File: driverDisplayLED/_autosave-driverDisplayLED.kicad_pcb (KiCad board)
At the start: 2 copper layers, 59 parts, among them J1 Conn_01x12_Male, J10 Conn_01x12_Male, J11 Conn_01x12_Male, J12 Conn_01x12_Male, J13 Conn_01x12_Male, J14 Conn_01x12_Male, J15 Conn_01x12_Male, J16 Conn_01x12_Male, J17 Conn_01x12_Male, J2 Conn_01x12_Male, J3 Conn_01x12_Male, J4 Conn_02x08_Counter_Clockwise, J5 Conn_01x12_Male, J6 Conn_01x12_Male, J7 Conn_01x12_Male, J8 Conn_01x12_Male, J9 Conn_01x12_Male, Q1 FDS4953, Q2 FDS4953, Q3 FDS4953, Q4 FDS4953, Q5 FDS4953, Q6 FDS4953, Q7 FDS4953, Q8 FDS4953, U1 74HC245, U2 74HC595, U3 74HC595, U4 74HC245, U5 74HC138D, U6 74HC04, U7 74HC595, U8 74HC595, U9 74HC138D

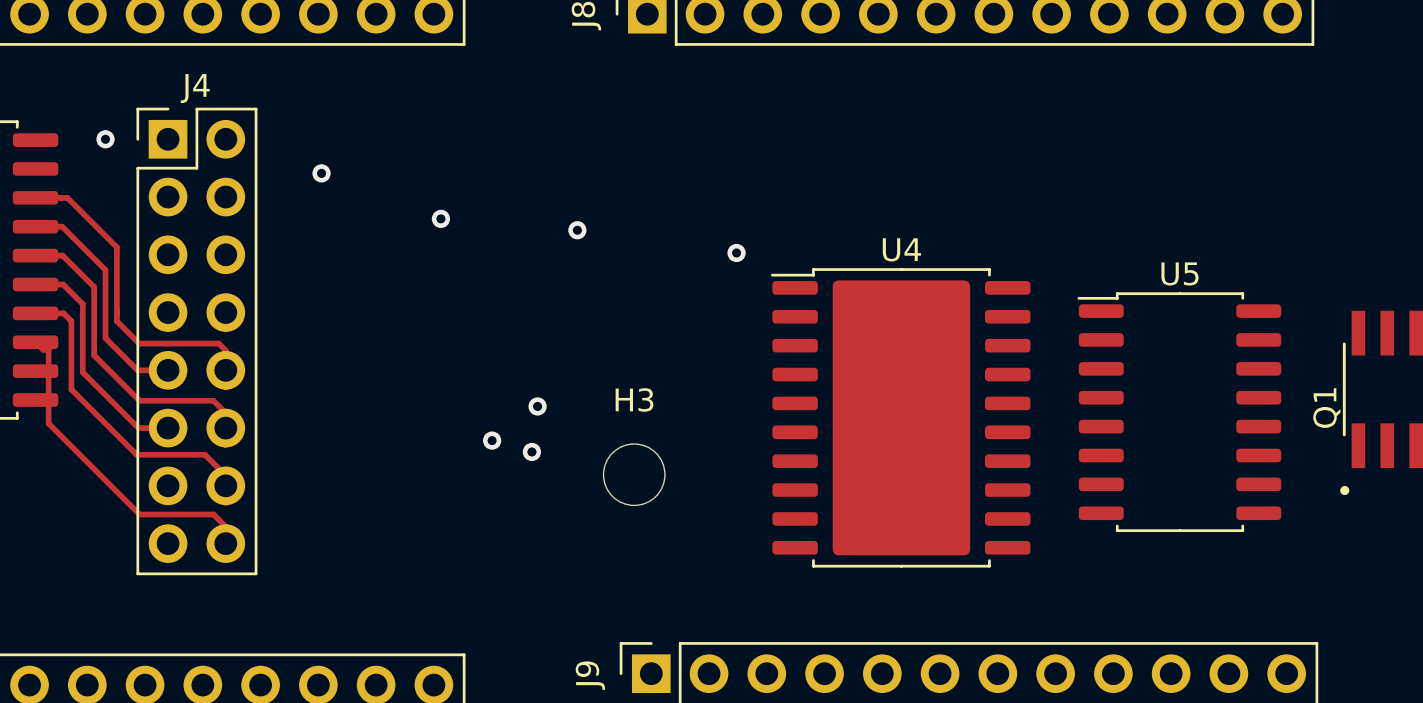
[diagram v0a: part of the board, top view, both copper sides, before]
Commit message: routing and mountholders
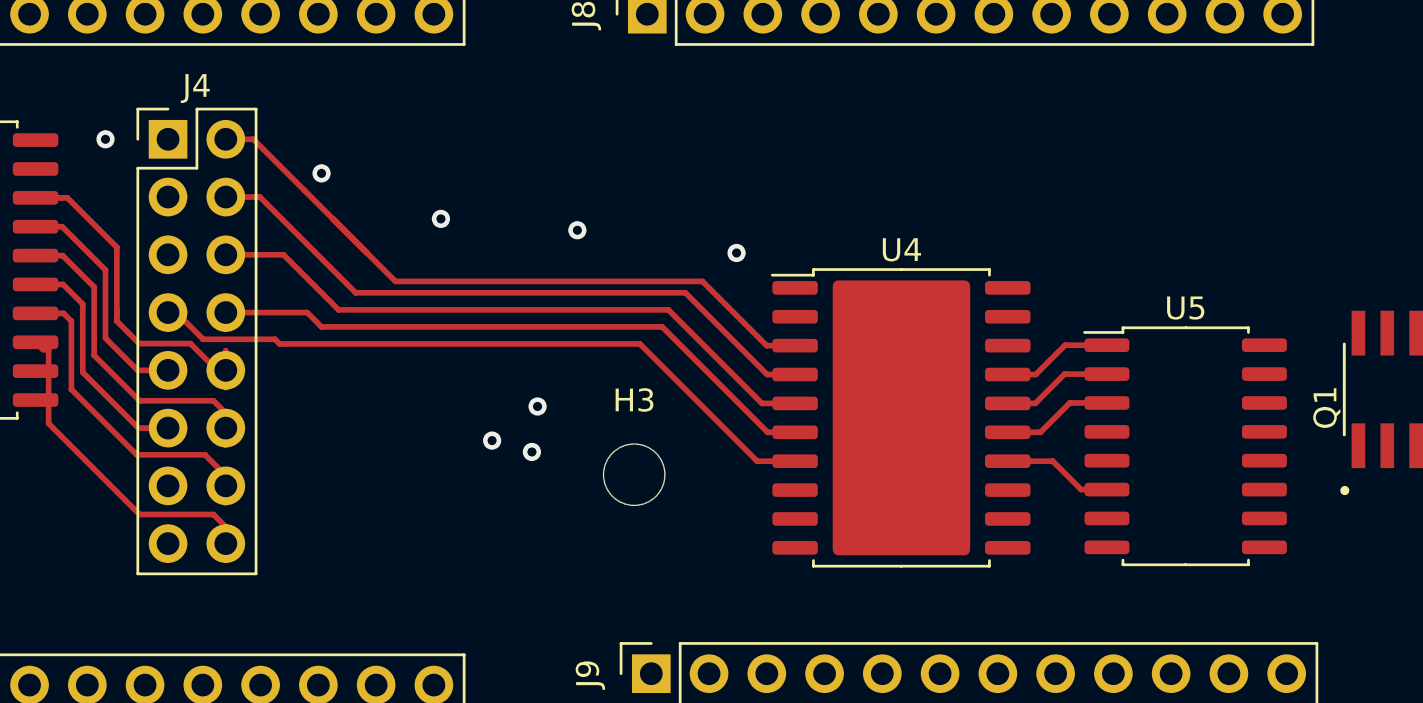
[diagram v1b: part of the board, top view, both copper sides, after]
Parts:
- moved U5 1.52 mm to (124.0, 119.5)
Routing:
- net Net-(J4-Pad2): track 0.00 -> 30.9 mm
- net /a4-A5: track 0.00 -> 30.3 mm
- net Net-(J4-Pad4): track 0.00 -> 28.3 mm
- net Net-(J4-Pad6): track 0.00 -> 27.7 mm
- net Net-(J4-Pad8): track 0.00 -> 27.2 mm
- net Net-(U4-Pad15): track 0.00 -> 4.90 mm
- net Net-(U4-Pad17): track 0.00 -> 4.90 mm
- net Net-(U4-Pad16): track 0.00 -> 4.90 mm
- net Net-(U4-Pad14): track 0.00 -> 4.88 mm
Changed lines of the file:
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@@
     (thickness 1.6)
     (drawings 108)
-    (tracks 91)
+    (tracks 134)
     (zones 0)
     (modules 59)
@@
   )
   (module Package_SO:SO-16_5.3x10.2mm_P1.27mm (layer F.Cu)
-    (at 123.75 118)
+    (at 124 119.5)
     (descr "SO, 16 Pin (https://www.ti.com/lit/ml/msop002a/msop002a.pdf), generated with kicad-footprint-generator ipc_gullwing_generator.py")
     (tags "SO SO")
@@
   (segment (start 77 110.75) (end 77 113.5) (width 0.25) (layer F.Cu) (net 8))
   (segment (start 77 113.5) (end 77 113.75) (width 0.25) (layer F.Cu) (net 8))
-  (segment (start 77.984999 114.984999) (end 81.484999 114.984999) (width 0.25) (layer F.Cu) (net 8))
   (segment (start 77 114) (end 77.984999 114.984999) (width 0.25) (layer F.Cu) (net 8))
   (segment (start 81.79 115.29) (end 81.79 116.16) (width 0.25) (layer F.Cu) (net 8))
-  (segment (start 81.484999 114.984999) (end 81.79 115.29) (width 0.25) (layer F.Cu) (net 8))
+  (segment (start 77.984999 114.984999) (end 80.234999 114.984999) (width 0.25) (layer F.Cu) (net 8))
+  (segment (start 81.41 116.16) (end 81.79 116.16) (width 0.25) (layer F.Cu) (net 8))
+  (segment (start 80.234999 114.984999) (end 81.41 116.16) (width 0.25) (layer F.Cu) (net 8))
   (segment (start 73.425 109.845) (end 74.595 109.845) (width 0.25) (layer F.Cu) (net 9))
   (segment (start 79.25 116.16) (end 77.91 116.16) (width 0.25) (layer F.Cu) (net 9))
@@
   (segment (start 112.25 70.75) (end 102.75 70.75) (width 0.25) (layer F.Cu) (net 19))
   (segment (start 117.5 70.75) (end 112.25 70.75) (width 0.25) (layer F.Cu) (net 19))
+  (segment (start 79.62 113.62) (end 79.25 113.62) (width 0.25) (layer F.Cu) (net 21))
+  (segment (start 80.795001 114.795001) (end 79.62 113.62) (width 0.25) (layer F.Cu) (net 21))
+  (segment (start 83.954999 114.795001) (end 80.795001 114.795001) (width 0.25) (layer F.Cu) (net 21))
+  (segment (start 84.159998 115) (end 83.954999 114.795001) (width 0.25) (layer F.Cu) (net 21))
+  (segment (start 100 115) (end 84.159998 115) (width 0.25) (layer F.Cu) (net 21))
+  (segment (start 105.155 120.155) (end 100 115) (width 0.25) (layer F.Cu) (net 21))
+  (segment (start 106.825 120.155) (end 105.155 120.155) (width 0.25) (layer F.Cu) (net 21))
+  (segment (start 116.175 118.885) (end 117.615 118.885) (width 0.25) (layer F.Cu) (net 26))
+  (segment (start 118.905 117.595) (end 120.5375 117.595) (width 0.25) (layer F.Cu) (net 26))
+  (segment (start 117.615 118.885) (end 118.905 117.595) (width 0.25) (layer F.Cu) (net 26))
+  (segment (start 116.175 117.615) (end 117.385 117.615) (width 0.25) (layer F.Cu) (net 27))
+  (segment (start 118.675 116.325) (end 120.5375 116.325) (width 0.25) (layer F.Cu) (net 27))
+  (segment (start 117.385 117.615) (end 118.675 116.325) (width 0.25) (layer F.Cu) (net 27))
+  (segment (start 116.175 116.345) (end 117.405 116.345) (width 0.25) (layer F.Cu) (net 28))
+  (segment (start 118.695 115.055) (end 120.5375 115.055) (width 0.25) (layer F.Cu) (net 28))
+  (segment (start 117.405 116.345) (end 118.695 115.055) (width 0.25) (layer F.Cu) (net 28))
+  (segment (start 116.175 120.155) (end 118.155 120.155) (width 0.25) (layer F.Cu) (net 40))
+  (segment (start 119.405 121.405) (end 120.5375 121.405) (width 0.25) (layer F.Cu) (net 40))
+  (segment (start 118.155 120.155) (end 119.405 121.405) (width 0.25) (layer F.Cu) (net 40))
   (segment (start 109.595 74.655) (end 109.595 73.5375) (width 0.25) (layer F.Cu) (net 140))
   (segment (start 109 75.25) (end 109.595 74.655) (width 0.25) (layer F.Cu) (net 140))
@@
   (segment (start 104.25 76.75) (end 105.75 75.25) (width 0.25) (layer F.Cu) (net 140))
   (segment (start 80.445 73.5375) (end 80.445 72.305) (width 0.25) (layer F.Cu) (net 140))
+  (segment (start 106.825 118.885) (end 105.615 118.885) (width 0.25) (layer F.Cu) (net 141))
+  (segment (start 105.615 118.885) (end 100.98 114.25) (width 0.25) (layer F.Cu) (net 141))
+  (segment (start 100.98 114.25) (end 86 114.25) (width 0.25) (layer F.Cu) (net 141))
+  (segment (start 85.37 113.62) (end 81.79 113.62) (width 0.25) (layer F.Cu) (net 141))
+  (segment (start 86 114.25) (end 85.37 113.62) (width 0.25) (layer F.Cu) (net 141))
+  (segment (start 81.79 111.08) (end 84.33 111.08) (width 0.25) (layer F.Cu) (net 142))
+  (segment (start 84.33 111.08) (end 86.75 113.5) (width 0.25) (layer F.Cu) (net 142))
+  (segment (start 86.75 113.5) (end 101.25 113.5) (width 0.25) (layer F.Cu) (net 142))
+  (segment (start 105.365 117.615) (end 106.825 117.615) (width 0.25) (layer F.Cu) (net 142))
+  (segment (start 101.25 113.5) (end 105.365 117.615) (width 0.25) (layer F.Cu) (net 142))
+  (segment (start 87.5 112.75) (end 83.29 108.54) (width 0.25) (layer F.Cu) (net 143))
+  (segment (start 83.29 108.54) (end 81.79 108.54) (width 0.25) (layer F.Cu) (net 143))
+  (segment (start 105.595 116.345) (end 102 112.75) (width 0.25) (layer F.Cu) (net 143))
+  (segment (start 102 112.75) (end 87.5 112.75) (width 0.25) (layer F.Cu) (net 143))
+  (segment (start 106.825 116.345) (end 105.595 116.345) (width 0.25) (layer F.Cu) (net 143))
+  (segment (start 81.79 106) (end 83 106) (width 0.25) (layer F.Cu) (net 144))
+  (segment (start 83 106) (end 85.25 108.25) (width 0.25) (layer F.Cu) (net 144))
+  (segment (start 106.825 115.075) (end 105.575 115.075) (width 0.25) (layer F.Cu) (net 144))
+  (segment (start 105.575 115.075) (end 102.75 112.25) (width 0.25) (layer F.Cu) (net 144))
+  (segment (start 89.25 112.25) (end 86.5 109.5) (width 0.25) (layer F.Cu) (net 144))
+  (segment (start 102.75 112.25) (end 89.25 112.25) (width 0.25) (layer F.Cu) (net 144))
+  (segment (start 86.5 109.5) (end 88 111) (width 0.25) (layer F.Cu) (net 144))
+  (segment (start 85.25 108.25) (end 86.5 109.5) (width 0.25) (layer F.Cu) (net 144))
   (zone (net 1) (net_name GND) (layer F.Cu) (hatch edge 0.508)
     (connect_pads (clearance 0.8))
